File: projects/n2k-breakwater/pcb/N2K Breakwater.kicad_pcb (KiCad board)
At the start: 4 copper layers, 68.2 x 43.1 mm, 45 parts, among them J1 Shield to Ground, J2 N2K, J3 Signals, J4 Power, Q1 SQJ872EP-T1_BE3, Q2 SQJ872EP-T1_BE3, Q3 BSS123NH6327XTSA1, Q4 BSS126H6327XTSA2

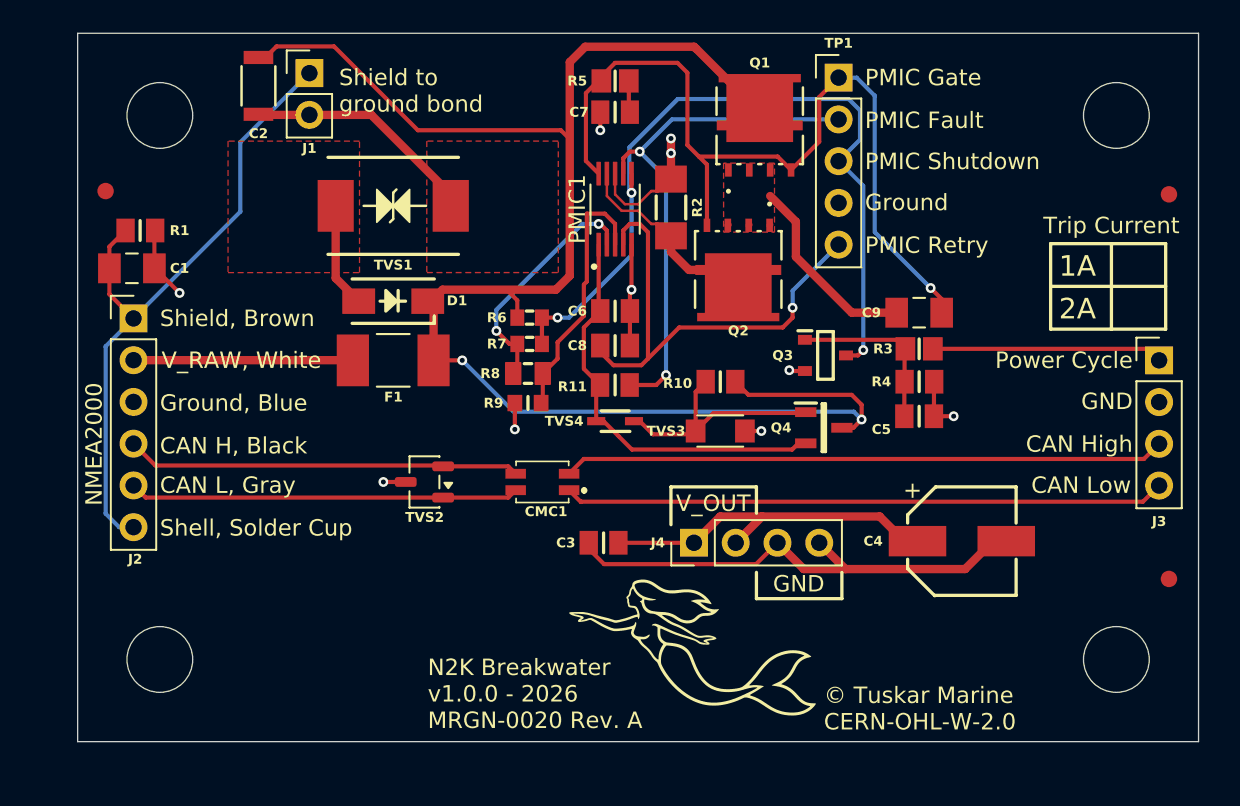
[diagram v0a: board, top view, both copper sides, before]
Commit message: Added zip-tie slots to allow strain relief.
Signed-off-by: digimer <digital.mermaid@gmail.com>
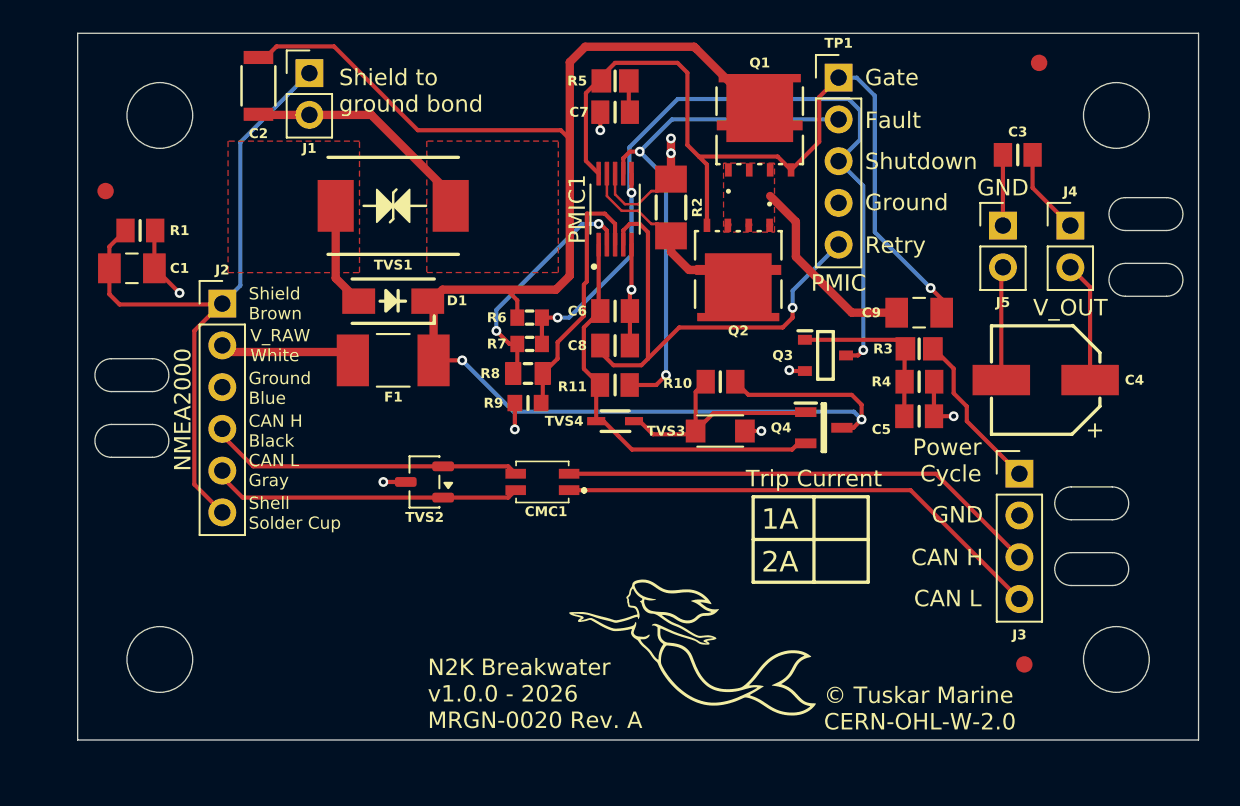
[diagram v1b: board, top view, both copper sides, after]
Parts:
- added J5: GND, Connector_PinHeader_2.54mm:PinHeader_1x02_P2.54mm_Vertical, F.Cu at (118.8, 86.7)
- added ZT1: ~, mr-stuff:Tuskar Ziptie Slot 4.5x2mm, F.Cu at (127.5, 86.0)
- added ZT2: ~, mr-stuff:Tuskar Ziptie Slot 4.5x2mm, F.Cu at (127.5, 90.0)
- added ZT3: ~, mr-stuff:Tuskar Ziptie Slot 4.5x2mm, F.Cu at (124.2, 103.6)
- added ZT4: ~, mr-stuff:Tuskar Ziptie Slot 4.5x2mm, F.Cu at (124.2, 107.6)
- added ZT5: ~, mr-stuff:Tuskar Ziptie Slot 4.5x2mm, F.Cu at (65.8, 95.8)
- added ZT6: ~, mr-stuff:Tuskar Ziptie Slot 4.5x2mm, F.Cu at (65.8, 99.8)
- J4: value Power -> V_RAW; footprint Connector_PinHeader_2.54mm:PinHeader_1x04_P2.54mm_Vertical -> Connector_PinHeader_2.54mm:PinHeader_1x02_P2.54mm_Vertical
- moved C3 34.5 mm to (119.7, 82.4)
- moved J4 29.9 mm to (122.9, 86.7), turned to 0 degrees
- moved FID1 11.2 mm to (121.0, 76.8)
- moved C4 11.0 mm to (121.4, 96.1), turned to 180 degrees
- moved J3 10.9 mm to (119.8, 101.8)
- moved FID2 10.2 mm to (120.1, 113.4)
- moved J2 5.47 mm to (71.3, 91.5)
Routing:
- net GND: track 64.8 -> 45.7 mm
- net V_OUT: track 24.2 -> 15.1 mm
- net /SAFE_CAN_H: track 36.7 -> 29.5 mm
- net /SAFE_CAN_L: track 36.6 -> 30.1 mm
- net /M12_CAN_L: track 23.7 -> 18.6 mm
- net /M12_V_RAW: track 13.3 -> 8.16 mm
- net /M12_CAN_H: track 24.0 -> 18.9 mm
- net /POWER_CYCLE: track 14.1 -> 9.82 mm
- net Net-(J1-Pin_1): track 40.3 -> 41.8 mm
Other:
- board size 68.2 x 43.1 mm -> 68.2 x 43 mm
- board text added: "CAN H"
- board text added: "CAN H Black"
- board text added: "CAN L"
- board text added: "CAN L Gray"
- board text added: "Fault"
- board text added: "Gate"
- board text added: "Ground Blue"
- board text added: "PMIC"
- board text added: "Retry"
- board text added: "Shell Solder Cup"
- board text added: "Shield Brown"
- board text added: "Shutdown"
- board text added: "V_RAW White"
- board text removed: "CAN H, Black"
- board text removed: "CAN High"
- board text removed: "CAN L, Gray"
- board text removed: "CAN Low"
- board text removed: "Ground, Blue"
- board text removed: "PMIC Fault"
- board text removed: "PMIC Gate"
- board text removed: "PMIC Retry"
- board text removed: "PMIC Shutdown"
- board text removed: "Shell, Solder Cup"
- board text removed: "Shield, Brown"
- board text removed: "V_RAW, White"

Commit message: Added some silkscreen flurish
Signed-off-by: digimer <digital.mermaid@gmail.com>
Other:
- board text added: "Ziptie"
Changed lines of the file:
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@@
 		)
+	)
+	(gr_circle
+		(center 67.5 80)
+		(end 67.5 84.2)
+		(stroke
+			(width 0.1)
+			(type default)
+		)
+		(fill no)
+		(layer "F.SilkS")
+	)
+	(gr_circle
+		(center 67.5 113.1)
+		(end 67.5 117.3)
+		(stroke
+			(width 0.1)
+			(type default)
+		)
+		(fill no)
+		(layer "F.SilkS")
 	)
 	(gr_rect
@@
 			(type solid)
 		)
+		(layer "F.SilkS")
+	)
+	(gr_circle
+		(center 125.7 80)
+		(end 125.7 84.2)
+		(stroke
+			(width 0.1)
+			(type default)
+		)
+		(fill no)
+		(layer "F.SilkS")
+	)
+	(gr_circle
+		(center 125.7 113.1)
+		(end 125.7 117.3)
+		(stroke
+			(width 0.1)
+			(type default)
+		)
+		(fill no)
 		(layer "F.SilkS")
 	)
@@
 		)
 	)
+	(gr_text "Ziptie"
+		(at 65.8 97.7 0)
+		(layer "F.SilkS")
+		(effects
+			(font
+				(size 0.75 0.75)
+				(thickness 0.1)
+			)
+		)
+	)
+	(gr_text "Ziptie"
+		(at 124.2 105.5 0)
+		(layer "F.SilkS")
+		(effects
+			(font
+				(size 0.75 0.75)
+				(thickness 0.1)
+			)
+		)
+	)
+	(gr_text "Ziptie"
+		(at 127.5 87.9 0)
+		(layer "F.SilkS")
+		(effects
+			(font
+				(size 0.75 0.75)
+				(thickness 0.1)
+			)
+		)
+	)

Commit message: Fixed DRC issues.
Signed-off-by: digimer <digital.mermaid@gmail.com>
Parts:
- moved REF** 0.20 mm to (81.6, 100.9)
- renumbered C9 to C3, C6 to C4, C7 to C5, C8 to C6, C3 to C7, C4 to C8, C5 to C9, Q4 to Q1, Q1 to Q2, Q2 to Q3, Q3 to Q4, R3 to R10, R4 to R11, R6 to R2, R7 to R3, R8 to R4, R9 to R5, R10 to R6, R2 to R7, R11 to R8, R5 to R9, TVS2 to TVS1, TVS1 to TVS2

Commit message: Increased spacing between solder points and ziptie slots.
Signed-off-by: digimer <digital.mermaid@gmail.com>
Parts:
- J4: value V_RAW -> V_OUT
- moved ZT3 3.20 mm to (127.4, 103.6)
- moved ZT4 3.20 mm to (127.4, 107.6)
- moved J2 1.30 mm to (72.6, 91.5)
- moved J4 1.24 mm to (121.7, 86.4)
- moved J5 1.24 mm to (117.6, 86.4)
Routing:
- net /M12_V_RAW: track 8.16 -> 7.02 mm
- net /M12_CAN_L: track 18.6 -> 17.4 mm
- net /M12_CAN_H: track 18.9 -> 17.8 mm
- net GND: track 45.7 -> 46.6 mm
- net Net-(J1-Pin_1): track 41.8 -> 42.5 mm
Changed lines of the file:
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@@
 	(footprint "Connector_PinHeader_2.54mm:PinHeader_1x02_P2.54mm_Vertical"
 		(layer "F.Cu")
-		(at 118.8 86.7)
+		(at 117.6 86.4)
 		(descr "Through hole straight pin header, 1x02, 2.54mm pitch, single row")
 		(tags "Through hole pin header THT 1x02 2.54mm single row")
 		(property "Reference" "J5"
-			(at 0 4.675 0)
+			(at 0 -2.1 0)
 			(layer "F.SilkS")
 			(effects
@@
 	(footprint "mr-stuff:Tuskar Ziptie Slot 4.5x2mm"
 		(layer "F.Cu")
-		(at 124.2 107.6)
+		(at 127.4 107.6)
 		(property "Reference" "ZT4"
 			(at 0 -1.6 0)
@@
 	(footprint "mr-stuff:Tuskar Ziptie Slot 4.5x2mm"
 		(layer "F.Cu")
-		(at 124.2 103.6)
+		(at 127.4 103.6)
 		(property "Reference" "ZT3"
 			(at 0 -1.6 0)
@@
 	(footprint "Connector_PinHeader_2.54mm:PinHeader_1x02_P2.54mm_Vertical"
 		(layer "F.Cu")
-		(at 122.9 86.7)
+		(at 121.7 86.4)
 		(descr "Through hole straight pin header, 1x02, 2.54mm pitch, single row")
 		(tags "Through hole pin header THT 1x02 2.54mm single row")
@@
 			)
 		)
-		(property "Value" "V_RAW"
+		(property "Value" "V_OUT"
 			(at 0 4.92 0)
 			(layer "F.Fab")
@@
 	(footprint "Connector_PinHeader_2.54mm:PinHeader_1x06_P2.54mm_Vertical"
 		(layer "F.Cu")
-		(at 71.3 91.45)
+		(at 72.6 91.45)
 		(descr "Through hole straight pin header, 1x06, 2.54mm pitch, single row")
 		(tags "Through hole pin header THT 1x06 2.54mm single row")
@@
 	)
 	(gr_text "Shield\nBrown"
-		(at 72.9 91.45 0)
+		(at 74.2 91.45 0)
 		(layer "F.SilkS")
 		(effects
@@
 	)
 	(gr_text "Ground\nBlue"
-		(at 72.9 96.6 0)
+		(at 74.2 96.6 0)
 		(layer "F.SilkS")
 		(effects
@@
 	)
 	(gr_text "CAN H\nBlack"
-		(at 72.9 99.2 0)
+		(at 74.2 99.2 0)
 		(layer "F.SilkS")
 		(effects
@@
 	)
 	(gr_text "CAN L\nGray"
-		(at 72.9 101.6 0)
+		(at 74.2 101.6 0)
 		(layer "F.SilkS")
 		(effects
@@
 	)
 	(gr_text "Shell\nSolder Cup"
-		(at 72.9 104.2 0)
+		(at 74.2 104.2 0)
 		(layer "F.SilkS")
 		(effects
@@
 	)
 	(gr_text "V_RAW\nWhite"
-		(at 73 94 0)
+		(at 74.3 94 0)
 		(layer "F.SilkS")
 		(effects
@@
 	)
 	(gr_text "Ziptie"
-		(at 124.2 105.5 0)
+		(at 127.4 105.5 0)
 		(layer "F.SilkS")
 		(effects
@@
 	)
 	(gr_text "GND"
-		(at 118.8 84.4 0)
+		(at 117.6 91.3 0)
 		(layer "F.SilkS")
 		(effects
@@
 	)
 	(gr_text "V_OUT"
-		(at 122.9 91.7 0)
+		(at 122.5 91.3 0)
 		(layer "F.SilkS")
 		(effects
@@
 	)
 	(gr_text "NMEA2000"
-		(at 68.9 97.9 90)
+		(at 70.2 97.9 90)
 		(layer "F.SilkS")
 		(effects
@@
 	)
 	(segment
-		(start 118.7983 82.4)
-		(end 118.7983 86.6983)
-		(width 0.254)
-		(layer "F.Cu")
-		(net "GND")
-	)
-	(segment
 		(start 73.537 79.965)
 		(end 73.5 79.928)
@@
 	)
 	(segment
+		(start 118.7 96.1)
+		(end 118.7 90)
+		(width 0.254)
+		(layer "F.Cu")
+		(net "GND")
+	)
+	(segment
+		(start 117.64 88.94)
+		(end 117.6 88.94)
+		(width 0.254)
+		(layer "F.Cu")
+		(net "GND")
+	)
+	(segment
 		(start 105.85 95.55)
 		(end 105.8 95.5)
@@
 	)
 	(segment
+		(start 118.7983 85.2017)
+		(end 117.6 86.4)
+		(width 0.254)
+		(layer "F.Cu")
+		(net "GND")
+	)
+	(segment
 		(start 73.5 79.928)
 		(end 73.463 79.965)
@@
 	)
 	(segment
+		(start 118.7983 82.4)
+		(end 118.7983 85.2017)
+		(width 0.254)
+		(layer "F.Cu")
+		(net "GND")
+	)
+	(segment
 		(start 96.1017 90.6983)
 		(end 96.2 90.6)
@@
 	)
 	(segment
-		(start 118.7 89.34)
-		(end 118.8 89.24)
-		(width 0.254)
-		(layer "F.Cu")
-		(net "GND")
-	)
-	(segment
-		(start 118.7983 86.6983)
-		(end 118.8 86.7)
+		(start 118.7 90)
+		(end 117.64 88.94)
 		(width 0.254)
 		(layer "F.Cu")
@@
 		(net "GND")
 	)
-	(segment
-		(start 118.7 96.1)
-		(end 118.7 89.34)
-		(width 0.254)
-		(layer "F.Cu")
-		(net "GND")
-	)
 	(via
 		(at 96.2 90.6)
@@
 	)
 	(segment
-		(start 69.6 93.1)
-		(end 69.6 102.45)
+		(start 70.9 93.1)
+		(end 70.9 102.45)
 		(width 0.254)
 		(layer "F.Cu")
@@
 	)
 	(segment
-		(start 71.25 91.45)
-		(end 69.6 93.1)
-		(width 0.254)
-		(layer "F.Cu")
-		(net "Net-(J1-Pin_1)")
-	)
-	(segment
-		(start 65.05 91.5)
-		(end 71.25 91.5)
+		(start 72.55 91.45)
+		(end 70.9 93.1)
 		(width 0.254)
 		(layer "F.Cu")
@@
 	)
 	(segment
-		(start 64.431 90.881)
-		(end 65.05 91.5)
+		(start 64.431 89.3)
+		(end 64.431 90.881)
 		(width 0.254)
 		(layer "F.Cu")
@@
 	)
 	(segment
-		(start 71.3 91.45)
-		(end 71.25 91.45)
+		(start 64.431 87.9818)
+		(end 65.4128 87)
 		(width 0.254)
 		(layer "F.Cu")
@@
 	)
 	(segment
-		(start 71.25 91.5)
-		(end 71.3 91.45)
+		(start 70.9 102.45)
+		(end 72.6 104.15)
 		(width 0.254)
 		(layer "F.Cu")
@@
 	)
 	(segment
-		(start 64.431 87.9818)
-		(end 65.4128 87)
+		(start 64.431 90.881)
+		(end 65.05 91.5)
 		(width 0.254)
 		(layer "F.Cu")
@@
 	)
 	(segment
-		(start 69.6 102.45)
-		(end 71.3 104.15)
+		(start 65.05 91.5)
+		(end 72.55 91.5)
 		(width 0.254)
 		(layer "F.Cu")
@@
 	)
 	(segment
-		(start 64.431 89.3)
-		(end 64.431 90.881)
+		(start 72.55 91.5)
+		(end 72.6 91.45)
 		(width 0.254)
 		(layer "F.Cu")
@@
 	)
 	(segment
-		(start 71.3 91.45)
-		(end 72.4 90.35)
+		(start 73.6 90.45)
+		(end 73.6 80.425)
 		(width 0.254)
 		(layer "B.Cu")
@@
 	)
 	(segment
-		(start 72.4 90.35)
-		(end 72.4 81.625)
+		(start 73.6 80.425)
+		(end 76.6 77.425)
 		(width 0.254)
 		(layer "B.Cu")
@@
 	)
 	(segment
-		(start 72.4 81.625)
-		(end 76.6 77.425)
+		(start 72.6 91.45)
+		(end 73.6 90.45)
 		(width 0.254)
 		(layer "B.Cu")
@@
 	)
 	(segment
+		(start 73 94.39)
+		(end 78.735 94.39)
+		(width 0.508)
+		(layer "F.Cu")
+		(net "/M12_V_RAW")
+	)
+	(segment
 		(start 78.735 94.39)
 		(end 79.245 94.9)
@@
 	)
 	(segment
-		(start 71.3 94.39)
-		(end 78.735 94.39)
+		(start 72.6 93.99)
+		(end 73 94.39)
 		(width 0.508)
 		(layer "F.Cu")
@@
 	)
 	(segment
-		(start 84.7375 103.25)
-		(end 72.54 103.25)
+		(start 88.7 103.25)
+		(end 89.15 102.8)
 		(width 0.254)
 		(layer "F.Cu")
@@
 	)
 	(segment
-		(start 88.7 103.25)
-		(end 89.15 102.8)
+		(start 74.24 103.25)
+		(end 72.6 101.61)
 		(width 0.254)
 		(layer "F.Cu")
@@
 	)
 	(segment
-		(start 72.54 103.25)
-		(end 71.3 102.01)
+		(start 84.7375 103.25)
+		(end 88.7 103.25)
 		(width 0.254)
 		(layer "F.Cu")
@@
 	(segment
 		(start 84.7375 103.25)
-		(end 88.7 103.25)
+		(end 74.24 103.25)
 		(width 0.254)
 		(layer "F.Cu")
@@
 	)
 	(segment
-		(start 88.7 101.35)
-		(end 89.15 101.8)
+		(start 84.7375 101.35)
+		(end 74.88 101.35)
 		(width 0.254)
 		(layer "F.Cu")
@@
 	)
 	(segment
-		(start 84.6875 101.3)
-		(end 84.7375 101.35)
+		(start 88.7 101.35)
+		(end 89.15 101.8)
 		(width 0.254)
 		(layer "F.Cu")
@@
 	)
 	(segment
-		(start 84.7375 101.35)
-		(end 88.7 101.35)
+		(start 74.88 101.35)
+		(end 72.6 99.07)
 		(width 0.254)
 		(layer "F.Cu")
@@
 	)
 	(segment
-		(start 73.18 101.35)
-		(end 71.3 99.47)
+		(start 84.6875 101.3)
+		(end 84.7375 101.35)
 		(width 0.254)
 		(layer "F.Cu")
@@
 	(segment
 		(start 84.7375 101.35)
-		(end 73.18 101.35)
+		(end 88.7 101.35)
 		(width 0.254)
 		(layer "F.Cu")
@@
 	)
 	(segment
-		(start 120.6017 82.4)
-		(end 120.6017 84.4017)
+		(start 121.7 88.94)
+		(end 124.1 91.34)
 		(width 0.254)
 		(layer "F.Cu")
@@
 	)
 	(segment
-		(start 124.1 90.44)
-		(end 124.1 96.1)
+		(start 120.6017 85.3017)
+		(end 121.9 86.6)
 		(width 0.254)
 		(layer "F.Cu")
@@
 	)
 	(segment
-		(start 122.9 89.24)
-		(end 124.1 90.44)
+		(start 120.6017 82.4)
+		(end 120.6017 85.3017)
 		(width 0.254)
 		(layer "F.Cu")
@@
 	)
 	(segment
-		(start 120.6017 84.4017)
-		(end 122.9 86.7)
+		(start 124.1 91.34)
+		(end 124.1 96.1)
 		(width 0.254)
 		(layer "F.Cu")

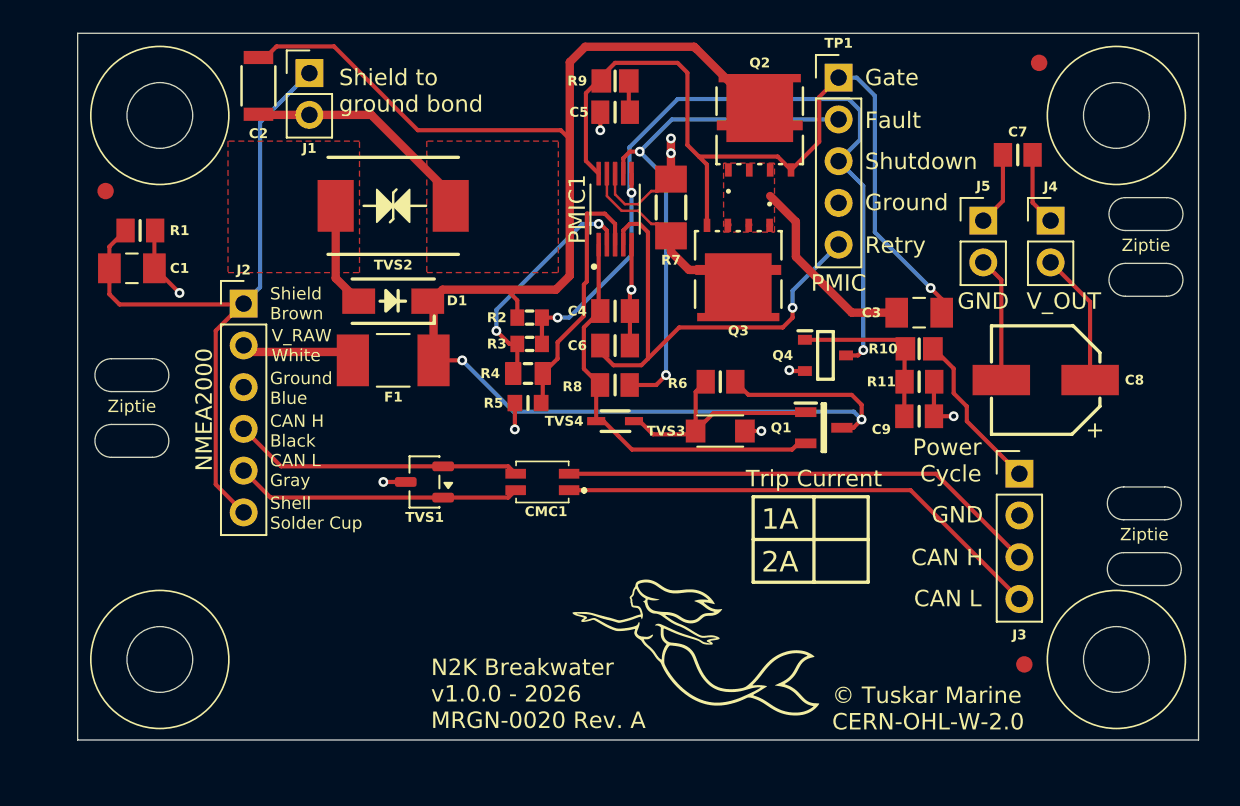
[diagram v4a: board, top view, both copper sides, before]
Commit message: Added a note and graphic to guide zip tie use.
Signed-off-by: digimer <digital.mermaid@gmail.com>
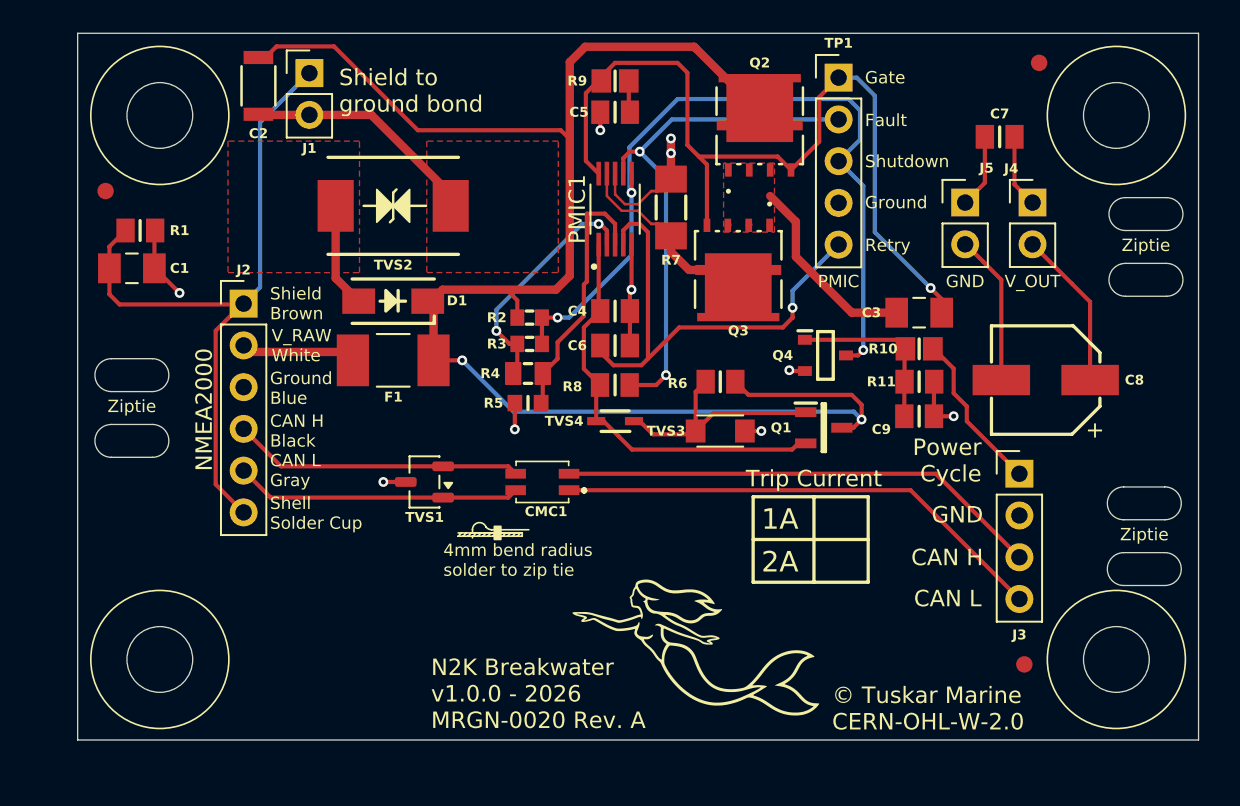
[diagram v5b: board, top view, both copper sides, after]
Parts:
- moved C7 1.56 mm to (118.6, 81.3)
- moved J4 1.56 mm to (120.6, 85.3)
- moved J5 1.56 mm to (116.5, 85.3)
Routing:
- net V_OUT: track 15.4 -> 16.9 mm
- net GND: track 46.6 -> 48.2 mm
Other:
- board text added: "4mm bend radius solder to zip tie"
